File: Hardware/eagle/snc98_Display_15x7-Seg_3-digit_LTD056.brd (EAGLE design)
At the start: 188.2 x 33.8 mm, 77 parts, among them M10 IRLML2244, M11 IRLML2244, M4 IRLML2244, M5 IRLML2244, M6 IRLML2244, M7 IRLML2244, M8 IRLML2244, M9 IRLML2244, X1 MICROMATCH-12, X2 MICROMATCH-14, X3 MICROMATCH-12, X4 MICROMATCH-14

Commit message: V 5.0 Hardware - Design
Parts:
- moved LED5 0.76 mm to (153.2, 24.1)
- moved LED1 0.51 mm to (1.78, 24.1)
- moved LED4 0.25 mm to (115.3, 24.1)
- moved LED2 0.25 mm to (39.6, 24.1)
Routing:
- net DIG_13: track 9.84 -> 7.74 mm
- net SEG_G: track 208.4 -> 209.4 mm
- net SEG_C: track 202.2 -> 203.2 mm
- net SEG_E: track 209.8 -> 210.4 mm
- net SEG_F: track 216.6 -> 217.1 mm
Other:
- board size 188.2 x 33.8 mm -> 190 x 33.8 mm

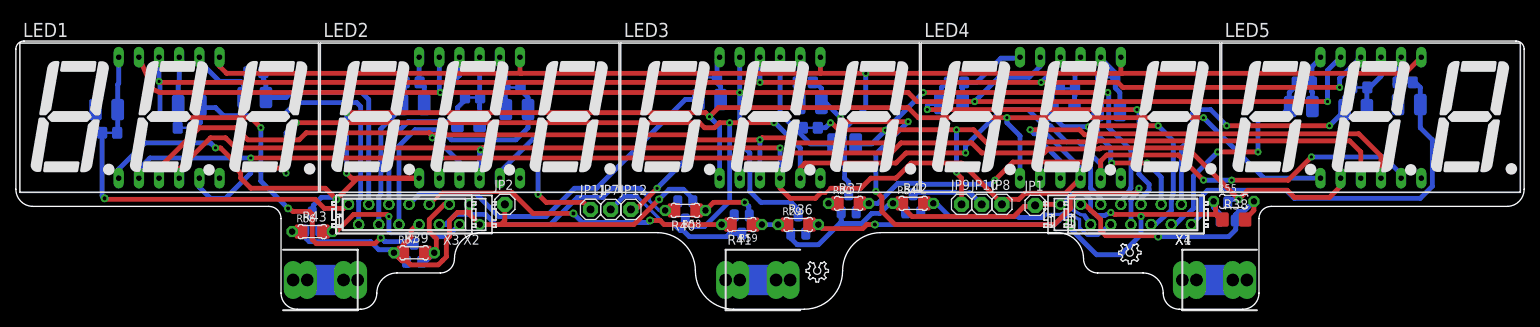
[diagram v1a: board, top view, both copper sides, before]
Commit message: PCB cleaning V1.1
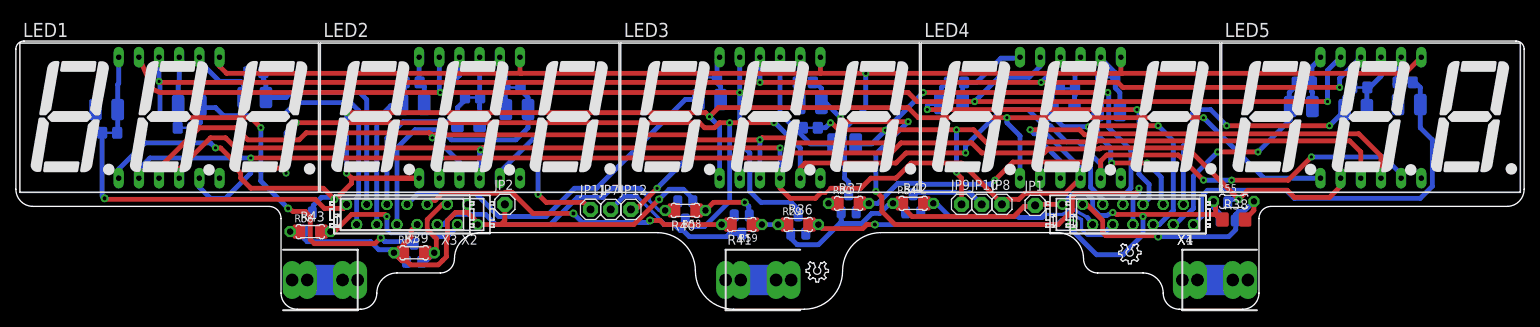
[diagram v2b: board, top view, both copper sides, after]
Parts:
- moved X1 0.25 mm to (123.8, 11.9)
- moved X2 0.25 mm to (32.4, 11.9)
- moved X4 0.25 mm to (122.6, 11.9)
- moved R43 0.25 mm to (19.6, 9.78)
- moved R56 0.25 mm to (19.6, 9.78)
- moved X3 0.25 mm to (31.1, 11.9)
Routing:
- net D12_A: track 29.8 -> 27.7 mm
- net D3_A: track 19.2 -> 20.5 mm
- net D1_A: track 40.0 -> 39.4 mm
- net IO-A: track 43.2 -> 43.7 mm
- net CA_LED: track 188.5 -> 189.0 mm

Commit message: sinh()_cosh()_tanh() added
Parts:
- moved LOGO3 2.84 mm to (127.0, 7.75)
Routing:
- net D13_A: track 37.4 -> 34.8 mm

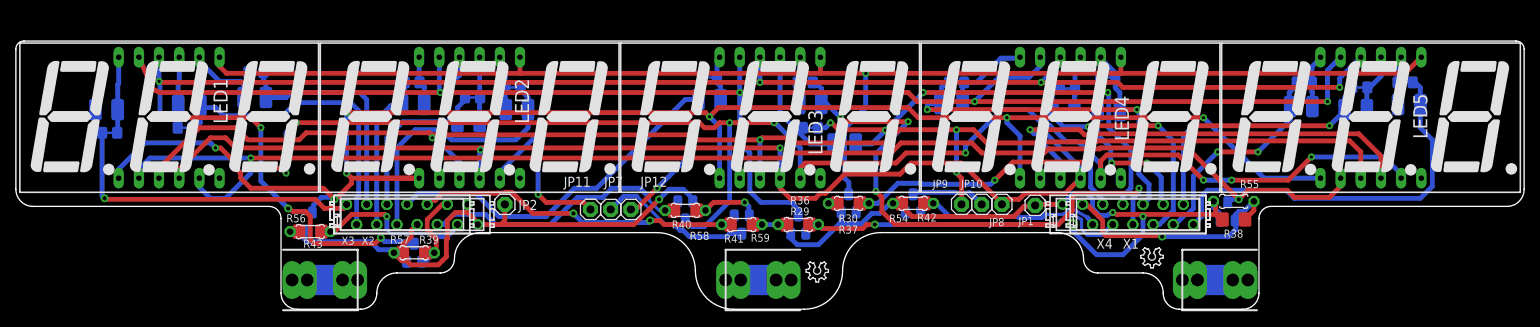
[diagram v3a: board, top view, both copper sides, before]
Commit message: PCB - add Tear Drop
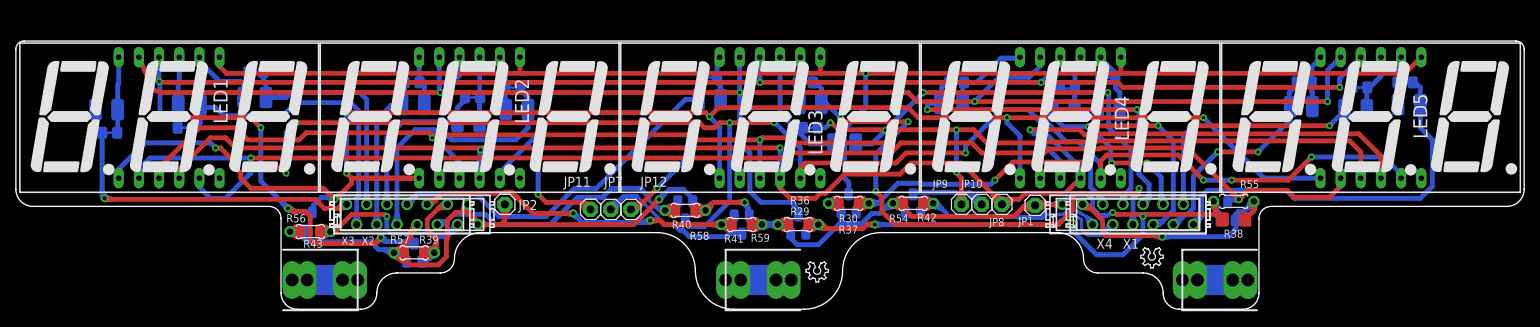
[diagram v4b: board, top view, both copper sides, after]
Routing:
- net CA_LED: track 189.0 -> 294.7 mm
- net IO-DP: track 43.2 -> 62.1 mm
- net IO-A: track 43.7 -> 57.8 mm
- net IO-D: track 30.4 -> 44.5 mm
- net SEG_C: track 203.2 -> 215.4 mm
- net IO-C: track 26.0 -> 35.9 mm
- net SEG_F: track 217.0 -> 226.5 mm
- net IO-G: track 36.6 -> 46.0 mm
- net IO-B: track 39.4 -> 48.8 mm
- net IO-E: track 22.2 -> 31.6 mm
- net IO-F: track 11.2 -> 20.5 mm
- net SEG_DP: track 201.9 -> 210.0 mm
- net D0_A: track 43.2 -> 51.1 mm
- net SEG_D: track 169.7 -> 176.9 mm
- net SEG_E: track 209.9 -> 217.1 mm
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
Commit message: Gerber file added
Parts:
- added R33, R34, R35, R44, R45, R46, R47, R48: 3k3, rcl:M0805
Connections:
- net CA_LED: now also R33.1, R34.1, R35.1, R44.1, R45.1, R46.1, R47.1, R48.1
- net IO-A: now also R33.2
- net IO-B: now also R34.2
- net IO-C: now also R47.2
- net IO-D: now also R35.2
- net IO-DP: now also R46.2
- net IO-E: now also R48.2
- net IO-F: now also R44.2
- net IO-G: now also R45.2
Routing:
- net CA_LED: track 294.7 -> 305.8 mm
- net IO-C: track 35.9 -> 38.4 mm
- net IO-A: track 57.8 -> 60.0 mm
- net IO-B: track 48.8 -> 50.7 mm
- net IO-E: track 31.6 -> 32.8 mm
- net IO-F: track 20.5 -> 21.5 mm

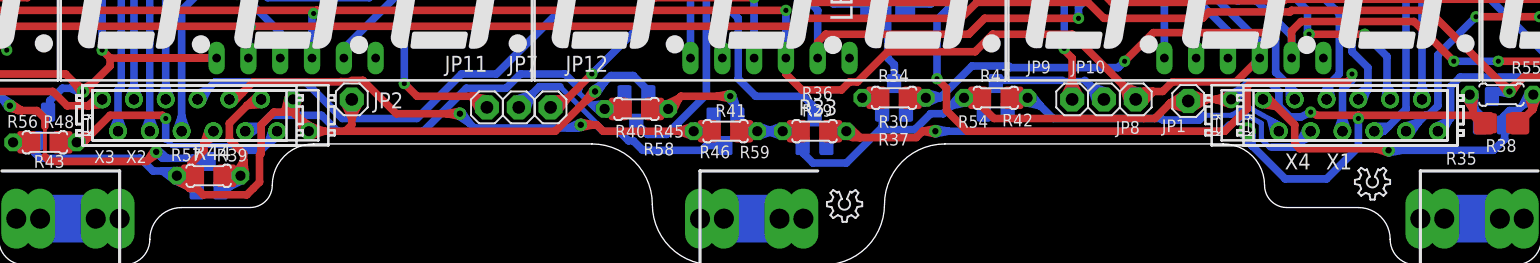
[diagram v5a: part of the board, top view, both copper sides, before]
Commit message: more accurate Factorial Function n!
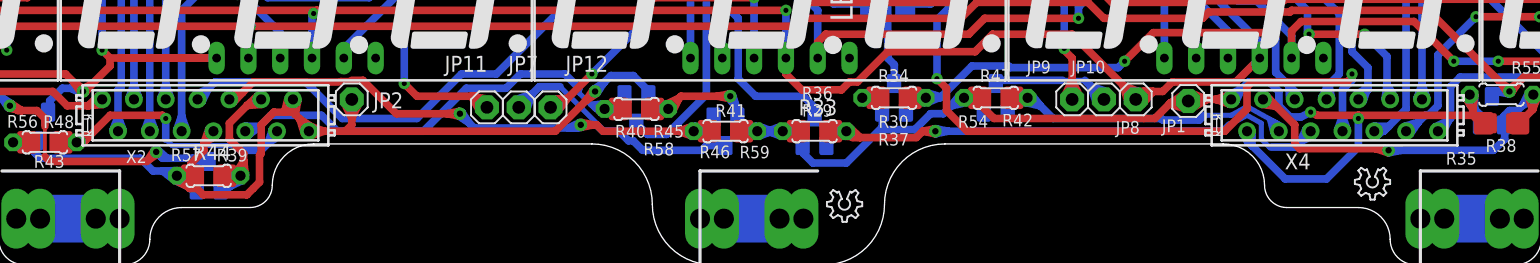
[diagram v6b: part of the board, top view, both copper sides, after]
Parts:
- removed X1, X3: MICROMATCH-12, Con-amp-micromatch:MICROMATCH-12
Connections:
- net CA_LED: no longer X3.8
- net D0_A: no longer X3.1
- net D10_A: no longer X1.8
- net D11_A: no longer X1.9
- net D12_A: no longer X1.10
- net D13_A: no longer X1.11
- net D14_A: no longer X1.12
- net D1_A: no longer X3.2
- net D2_A: no longer X3.3
- net D3_A: no longer X3.4
- net D4_A: no longer X3.5
- net D5_A: no longer X3.6
- net D6_A: no longer X3.7
- net D7_A: no longer X1.5
- net D8_A: no longer X1.6
- net D9_A: no longer X1.7
- net IO-A: no longer X1.4
- net IO-B: no longer X1.3
- net IO-C: no longer X1.2
- net IO-D: no longer X1.1
- net IO-DP: no longer X3.9
- net IO-E: no longer X3.12
- net IO-F: no longer X3.11
- net IO-G: no longer X3.10
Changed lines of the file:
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@@
 <setting verticaltext="up"/>
 </settings>
-<grid distance="5" unitdist="mil" unit="mil" style="lines" multiple="1" display="yes" altdistance="0.01" altunitdist="inch" altunit="inch"/>
+<grid distance="0.1" unitdist="inch" unit="inch" style="lines" multiple="1" display="yes" altdistance="0.01" altunitdist="inch" altunit="inch"/>
 <layers>
 <layer number="1" name="Top" color="4" fill="1" visible="yes" active="yes"/>
@@
 <attribute name="MPN" value="" x="19.558" y="9.779" size="1.778" layer="27" display="off"/>
 </element>
-<element name="X1" library="Con-amp-micromatch" package="MICROMATCH-12" value="MICROMATCH-12" x="123.825" y="11.938" locked="yes" smashed="yes" rot="R180">
-<attribute name="OC_NEWARK" value="95H9857" x="123.825" y="11.938" size="1.778" layer="27" rot="R180" display="off"/>
-<attribute name="MPN" value="8-215464-2" x="123.825" y="11.938" size="1.778" layer="27" rot="R180" display="off"/>
-<attribute name="MF" value="AMP - TE CONNECTIVITY" x="123.825" y="11.938" size="1.778" layer="27" rot="R180" display="off"/>
-<attribute name="OC_FARNELL" value="3784666" x="123.825" y="11.938" size="1.778" layer="27" rot="R180" display="off"/>
-<attribute name="NAME" x="123.952" y="8.89" size="1.27" layer="25" ratio="16" rot="R180"/>
-<attribute name="VALUE" x="130.81" y="15.748" size="1.27" layer="27" rot="R180"/>
-</element>
-<element name="X3" library="Con-amp-micromatch" package="MICROMATCH-12" value="MICROMATCH-12" x="31.115" y="11.938" locked="yes" smashed="yes" rot="R180">
-<attribute name="OC_NEWARK" value="95H9857" x="31.115" y="11.938" size="1.778" layer="27" rot="R180" display="off"/>
-<attribute name="MPN" value="8-215464-2" x="31.115" y="11.938" size="1.778" layer="27" rot="R180" display="off"/>
-<attribute name="MF" value="AMP - TE CONNECTIVITY" x="31.115" y="11.938" size="1.778" layer="27" rot="R180" display="off"/>
-<attribute name="OC_FARNELL" value="3784666" x="31.115" y="11.938" size="1.778" layer="27" rot="R180" display="off"/>
-<attribute name="NAME" x="25.146" y="9.144" size="1.016" layer="25" ratio="16" rot="R180"/>
-<attribute name="VALUE" x="38.1" y="15.748" size="1.27" layer="27" rot="R180"/>
-</element>
 <element name="JP7" library="adafruit" package="1X01" value="" x="57.404" y="12.573" locked="yes" smashed="yes">
 <attribute name="NAME" x="56.5658" y="15.4178" size="1.27" layer="25" ratio="16"/>
@@
 <contactref element="R36" pad="2"/>
 <contactref element="R29" pad="2"/>
-<contactref element="X1" pad="4"/>
 <wire x1="81.9785" y1="9.525" x2="81.9658" y2="10.1858" width="0.6096" layer="16"/>
 <wire x1="83.566" y1="10.668" x2="82.448" y2="10.668" width="0.6096" layer="1"/>
@@
 <contactref element="R37" pad="2"/>
 <contactref element="R30" pad="2"/>
-<contactref element="X1" pad="3"/>
 <wire x1="88.3285" y1="12.192" x2="88.3158" y2="12.8528" width="0.6096" layer="16"/>
 <wire x1="88.3158" y1="12.8528" x2="88.7006875" y2="13.2376875" width="0.6096" layer="16"/>
@@
 <contactref element="R38" pad="2"/>
 <contactref element="R55" pad="2"/>
-<contactref element="X1" pad="1"/>
 <wire x1="116.84" y1="13.208" x2="117.348" y2="13.208" width="0.6096" layer="1"/>
 <wire x1="119.38" y1="11.176" x2="119.38" y2="9.652" width="0.6096" layer="1"/>
@@
 <contactref element="R41" pad="2"/>
 <contactref element="R59" pad="2"/>
-<contactref element="X3" pad="9"/>
 <wire x1="71.374" y1="10.668" x2="72.492" y2="10.668" width="0.6096" layer="16"/>
 <wire x1="72.492" y1="10.668" x2="71.374" y2="10.668" width="0.6096" layer="1"/>
@@
 <contactref element="R43" pad="2"/>
 <contactref element="R56" pad="2"/>
-<contactref element="X3" pad="12"/>
 <via x="29.21" y="11.684" extent="1-16" drill="0.4"/>
 <wire x1="22.098" y1="9.779" x2="20.98" y2="9.779" width="0.6096" layer="1"/>
@@
 <contactref element="R39" pad="2"/>
 <contactref element="R57" pad="2"/>
-<contactref element="X3" pad="11"/>
 <wire x1="33.5915" y1="5.969" x2="34.163" y2="6.096" width="0.6096" layer="16"/>
 <wire x1="34.163" y1="6.096" x2="34.31689375" y2="6.24989375" width="0.6096" layer="16"/>
@@
 <contactref element="R40" pad="2"/>
 <contactref element="R58" pad="2"/>
-<contactref element="X3" pad="10"/>
 <wire x1="49.784" y1="10.668" x2="53.213" y2="14.097" width="0.6096" layer="16"/>
 <wire x1="53.213" y1="14.097" x2="56.388" y2="14.097" width="0.6096" layer="16"/>
@@
 <contactref element="R42" pad="2"/>
 <contactref element="R54" pad="2"/>
-<contactref element="X1" pad="2"/>
 <wire x1="96.926" y1="13.335" x2="97.561" y2="13.31" width="0.6096" layer="1"/>
 <wire x1="97.561" y1="13.31" x2="98.044" y2="13.335" width="0.6096" layer="1"/>
@@
 <contactref element="R42" pad="1"/>
 <contactref element="R43" pad="1"/>
-<contactref element="X3" pad="8"/>
 <contactref element="R29" pad="1"/>
 <contactref element="R30" pad="1"/>
@@
 <signal name="D0_A">
 <contactref element="R5" pad="2"/>
-<contactref element="X3" pad="1"/>
 <wire x1="20.193" y1="13.843" x2="-5.34196875" y2="13.843" width="0.6096" layer="1"/>
 <wire x1="-5.34196875" y1="13.843" x2="-6.223" y2="13.843" width="0.6096" layer="1"/>
@@
 <signal name="D1_A">
 <contactref element="R6" pad="2"/>
-<contactref element="X3" pad="2"/>
 <contactref element="X2" pad="2"/>
 <wire x1="25.654" y1="14.224" x2="25.654" y2="25.019" width="0.6096" layer="16"/>
@@
 <signal name="D2_A">
 <contactref element="R7" pad="2"/>
-<contactref element="X3" pad="3"/>
 <contactref element="X2" pad="3"/>
 <wire x1="13.973" y1="26.67" x2="13.973" y2="26.032" width="0.6096" layer="16"/>
@@
 <signal name="D4_A">
 <contactref element="R9" pad="2"/>
-<contactref element="X3" pad="5"/>
 <contactref element="X2" pad="5"/>
 <wire x1="38.097" y1="23.622" x2="31.242" y2="23.622" width="0.6096" layer="16"/>
@@
 <signal name="D5_A">
 <contactref element="R10" pad="2"/>
-<contactref element="X3" pad="6"/>
 <contactref element="X2" pad="6"/>
 <contactref element="R21" pad="2"/>
@@
 <signal name="D6_A">
 <contactref element="R11" pad="2"/>
-<contactref element="X3" pad="7"/>
 <contactref element="X2" pad="7"/>
 <wire x1="49.276" y1="11.684" x2="52.832" y2="15.24" width="0.6096" layer="16"/>
@@
 <signal name="D7_A">
 <contactref element="R12" pad="2"/>
-<contactref element="X1" pad="5"/>
 <contactref element="X4" pad="7"/>
 <via x="96.774" y="27.305" extent="1-16" drill="0.4064"/>
@@
 <signal name="D8_A">
 <contactref element="R13" pad="2"/>
-<contactref element="X1" pad="6"/>
 <contactref element="X4" pad="8"/>
 <wire x1="84.582" y1="25.908" x2="83.95" y2="25.908" width="0.6096" layer="16"/>
@@
 <signal name="D9_A">
 <contactref element="R14" pad="2"/>
-<contactref element="X1" pad="7"/>
 <contactref element="X4" pad="9"/>
 <via x="123.698" y="25.146" extent="1-16" drill="0.4064"/>
@@
 <signal name="D10_A">
 <contactref element="R15" pad="2"/>
-<contactref element="X1" pad="8"/>
 <contactref element="X4" pad="10"/>
 <contactref element="R26" pad="2"/>
@@
 <signal name="D11_A">
 <contactref element="R16" pad="2"/>
-<contactref element="X1" pad="9"/>
 <contactref element="X4" pad="11"/>
 <via x="124.968" y="18.415" extent="1-16" drill="0.4064"/>
@@
 <signal name="D12_A">
 <contactref element="R17" pad="2"/>
-<contactref element="X1" pad="10"/>
 <contactref element="X4" pad="12"/>
 <contactref element="R28" pad="2"/>
@@
 <signal name="D13_A">
 <contactref element="R18" pad="2"/>
-<contactref element="X1" pad="11"/>
 <contactref element="X4" pad="13"/>
 <wire x1="149.857" y1="25.146" x2="149.733" y2="25.146" width="0.6096" layer="16"/>
@@
 </signal>
 <signal name="D3_A">
-<contactref element="X3" pad="4"/>
 <contactref element="R8" pad="2"/>
 <contactref element="X2" pad="4"/>
@@
 <signal name="D14_A">
 <contactref element="R19" pad="2"/>
-<contactref element="X1" pad="12"/>
 <contactref element="X4" pad="14"/>
 <contactref element="R32" pad="2"/>

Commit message: cleanup_PCB
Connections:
- net SEG_C: no longer JP8.1
- net SEG_C_SOURCE: now also JP8.1
- net SEG_DP: now also JP7.1
- net SEG_DP_SOURCE: no longer JP7.1
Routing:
- net CA_LED: track 305.8 -> 625.4 mm
- net IO-DP: track 62.5 -> 116.3 mm
- net IO-A: track 60.0 -> 103.0 mm
- net IO-D: track 44.9 -> 83.4 mm
- net SEG_DP: track 210.0 -> 241.9 mm
- net IO-C: track 38.4 -> 69.5 mm
- net IO-B: track 50.7 -> 81.6 mm
- net IO-G: track 46.4 -> 74.9 mm
- net IO-E: track 32.8 -> 60.7 mm
- net IO-F: track 21.5 -> 49.4 mm
- net SEG_F: track 226.6 -> 253.1 mm
- net D0_A: track 51.1 -> 72.3 mm
- net SEG_C_SOURCE: track 13.4 -> 33.8 mm
- net SEG_E: track 217.1 -> 237.3 mm
- net SEG_D: track 176.9 -> 196.3 mm
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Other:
- board text added: "CERN OHL v.1.3"
- board text removed: "CERN OHL v.1.2"
